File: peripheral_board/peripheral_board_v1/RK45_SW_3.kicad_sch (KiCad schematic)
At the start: 10 parts

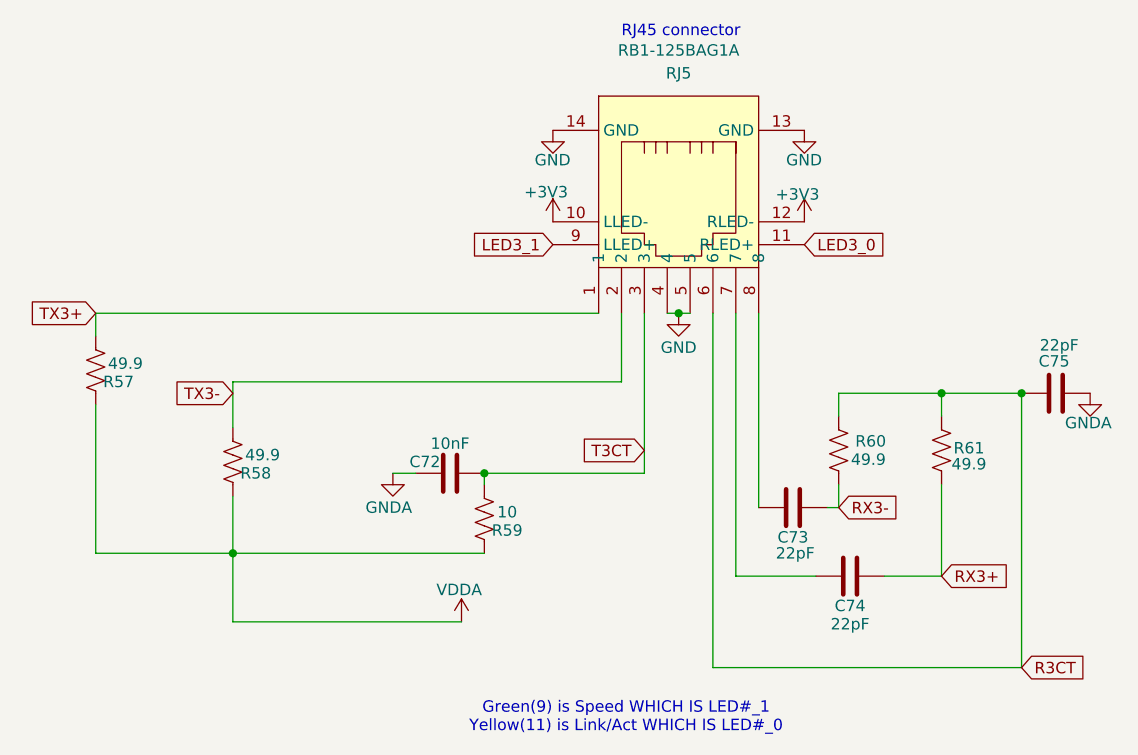
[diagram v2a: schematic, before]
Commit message: Schematic design ready for review
Made the last changes for the Wiznet by adding in Dip switches and made sure that the interrupt and reset signals are attached to the raspberry pi.

Finished the Etherent switch by wiring the RJ45 port 1 with 2 configurations, leaning more towards not using the Wiznet port but might do it any ways for cost. Added test points to port 5 but might change it to be RMII configuration because the 4 port strap in mode sets it to that config. Put solder jumpers in for the LED strap in mode. On the schematic I put in a note about how to configure to the proper mode we want but after a review will change to be a hardwire set. Made the reset switch match that of the EVAL board but further reading found I do not need the diode. Created the VDDIO and VDDAT which are just 2 different versions of 3.3V. Layout would be next but need to learn more about trace integrity and impedance control.
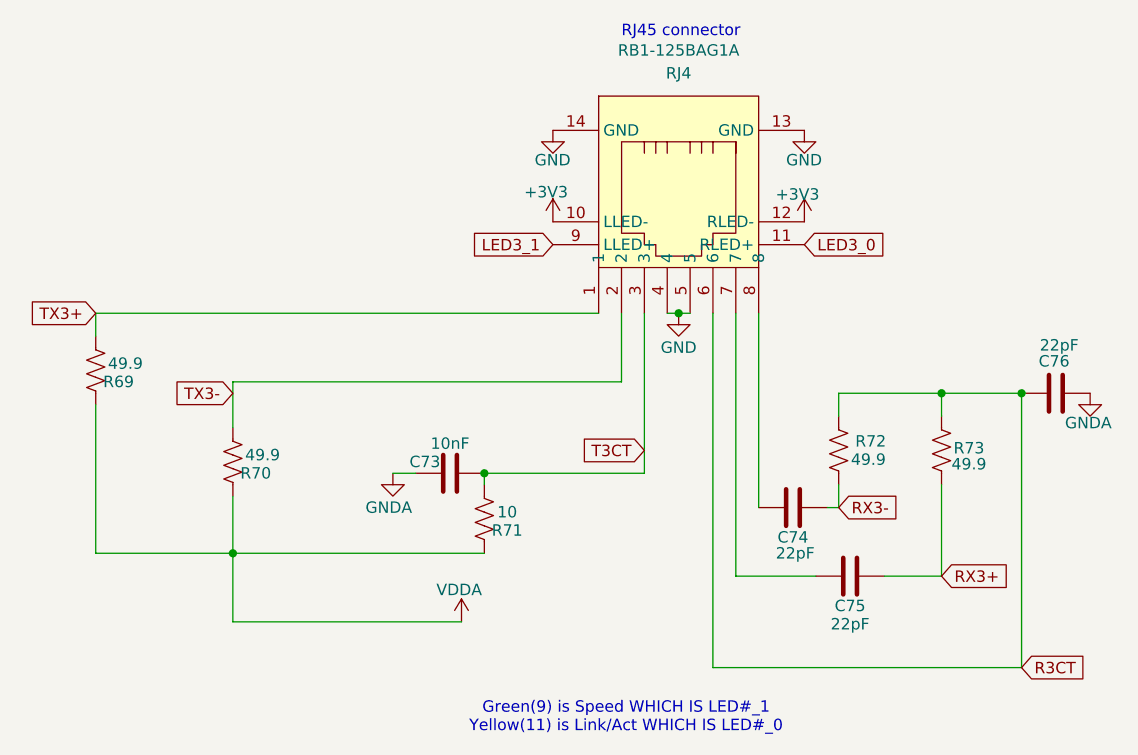
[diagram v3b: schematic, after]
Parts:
- renumbered C72 to C73, C73 to C74, C74 to C75, C75 to C76, R57 to R69, R58 to R70, R59 to R71, R60 to R72, R61 to R73, RJ5 to RJ4
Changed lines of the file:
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@@
 		(on_board yes)
 		(dnp no)
-		(property "Reference" "#PWR0139"
+		(property "Reference" "#PWR0162"
 			(at 236.22 123.19 0)
 			(effects
@@
 			(project "peripheral_board"
 				(path "/14f8712f-1710-40cb-b01e-cc9b3c4405bd/bdffb641-9271-40a7-b849-e20d9ae38619/bd5ccff9-e43e-4cae-813e-2c44e5ae50a7"
-					(reference "#PWR0139")
+					(reference "#PWR0162")
 					(unit 1)
 				)
@@
 		(on_board yes)
 		(dnp no)
-		(property "Reference" "R60"
+		(property "Reference" "R72"
 			(at 257.556 131.064 0)
 			(effects
@@
 			(project "peripheral_board"
 				(path "/14f8712f-1710-40cb-b01e-cc9b3c4405bd/bdffb641-9271-40a7-b849-e20d9ae38619/bd5ccff9-e43e-4cae-813e-2c44e5ae50a7"
-					(reference "R60")
+					(reference "R72")
 					(unit 1)
 				)
@@
 		(on_board yes)
 		(dnp no)
-		(property "Reference" "R57"
+		(property "Reference" "R69"
 			(at 173.99 124.46 0)
 			(effects
@@
 			(project "peripheral_board"
 				(path "/14f8712f-1710-40cb-b01e-cc9b3c4405bd/bdffb641-9271-40a7-b849-e20d9ae38619/bd5ccff9-e43e-4cae-813e-2c44e5ae50a7"
-					(reference "R57")
+					(reference "R69")
 					(unit 1)
 				)
@@
 		(dnp no)
 		(fields_autoplaced yes)
-		(property "Reference" "RJ5"
+		(property "Reference" "RJ4"
 			(at 236.22 90.17 0)
 			(effects
@@
 			(project "peripheral_board"
 				(path "/14f8712f-1710-40cb-b01e-cc9b3c4405bd/bdffb641-9271-40a7-b849-e20d9ae38619/bd5ccff9-e43e-4cae-813e-2c44e5ae50a7"
-					(reference "RJ5")
+					(reference "RJ4")
 					(unit 1)
 				)
@@
 		(on_board yes)
 		(dnp no)
-		(property "Reference" "C74"
+		(property "Reference" "C75"
 			(at 255.27 149.352 90)
 			(effects
@@
 			(project "peripheral_board"
 				(path "/14f8712f-1710-40cb-b01e-cc9b3c4405bd/bdffb641-9271-40a7-b849-e20d9ae38619/bd5ccff9-e43e-4cae-813e-2c44e5ae50a7"
-					(reference "C74")
+					(reference "C75")
 					(unit 1)
 				)
@@
 		(on_board yes)
 		(dnp no)
-		(property "Reference" "C75"
+		(property "Reference" "C76"
 			(at 279.654 122.174 90)
 			(effects
@@
 			(project "peripheral_board"
 				(path "/14f8712f-1710-40cb-b01e-cc9b3c4405bd/bdffb641-9271-40a7-b849-e20d9ae38619/bd5ccff9-e43e-4cae-813e-2c44e5ae50a7"
-					(reference "C75")
+					(reference "C76")
 					(unit 1)
 				)
@@
 		(on_board yes)
 		(dnp no)
-		(property "Reference" "R58"
+		(property "Reference" "R70"
 			(at 189.23 134.62 0)
 			(effects
@@
 			(project "peripheral_board"
 				(path "/14f8712f-1710-40cb-b01e-cc9b3c4405bd/bdffb641-9271-40a7-b849-e20d9ae38619/bd5ccff9-e43e-4cae-813e-2c44e5ae50a7"
-					(reference "R58")
+					(reference "R70")
 					(unit 1)
 				)
@@
 		(on_board yes)
 		(dnp no)
-		(property "Reference" "#PWR0137"
+		(property "Reference" "#PWR0160"
 			(at 222.25 102.87 0)
 			(effects
@@
 			(project "peripheral_board"
 				(path "/14f8712f-1710-40cb-b01e-cc9b3c4405bd/bdffb641-9271-40a7-b849-e20d9ae38619/bd5ccff9-e43e-4cae-813e-2c44e5ae50a7"
-					(reference "#PWR0137")
+					(reference "#PWR0160")
 					(unit 1)
 				)
@@
 		(on_board yes)
 		(dnp no)
-		(property "Reference" "R59"
+		(property "Reference" "R71"
 			(at 217.17 140.97 0)
 			(effects
@@
 			(project "peripheral_board"
 				(path "/14f8712f-1710-40cb-b01e-cc9b3c4405bd/bdffb641-9271-40a7-b849-e20d9ae38619/bd5ccff9-e43e-4cae-813e-2c44e5ae50a7"
-					(reference "R59")
+					(reference "R71")
 					(unit 1)
 				)
@@
 		(on_board yes)
 		(dnp no)
-		(property "Reference" "#PWR0141"
+		(property "Reference" "#PWR0164"
 			(at 250.19 110.49 0)
 			(effects
@@
 			(project "peripheral_board"
 				(path "/14f8712f-1710-40cb-b01e-cc9b3c4405bd/bdffb641-9271-40a7-b849-e20d9ae38619/bd5ccff9-e43e-4cae-813e-2c44e5ae50a7"
-					(reference "#PWR0141")
+					(reference "#PWR0164")
 					(unit 1)
 				)
@@
 		(on_board yes)
 		(dnp no)
-		(property "Reference" "#PWR0136"
+		(property "Reference" "#PWR0159"
 			(at 212.09 154.94 0)
 			(effects
@@
 			(project "peripheral_board"
 				(path "/14f8712f-1710-40cb-b01e-cc9b3c4405bd/bdffb641-9271-40a7-b849-e20d9ae38619/bd5ccff9-e43e-4cae-813e-2c44e5ae50a7"
-					(reference "#PWR0136")
+					(reference "#PWR0159")
 					(unit 1)
 				)
@@
 		(on_board yes)
 		(dnp no)
-		(property "Reference" "#PWR0138"
+		(property "Reference" "#PWR0161"
 			(at 222.25 110.49 0)
 			(effects
@@
 			(project "peripheral_board"
 				(path "/14f8712f-1710-40cb-b01e-cc9b3c4405bd/bdffb641-9271-40a7-b849-e20d9ae38619/bd5ccff9-e43e-4cae-813e-2c44e5ae50a7"
-					(reference "#PWR0138")
+					(reference "#PWR0161")
 					(unit 1)
 				)
@@
 		(on_board yes)
 		(dnp no)
-		(property "Reference" "C73"
+		(property "Reference" "C74"
 			(at 248.92 141.732 90)
 			(effects
@@
 			(project "peripheral_board"
 				(path "/14f8712f-1710-40cb-b01e-cc9b3c4405bd/bdffb641-9271-40a7-b849-e20d9ae38619/bd5ccff9-e43e-4cae-813e-2c44e5ae50a7"
-					(reference "C73")
+					(reference "C74")
 					(unit 1)
 				)
@@
 		(on_board yes)
 		(dnp no)
-		(property "Reference" "R61"
+		(property "Reference" "R73"
 			(at 268.478 131.826 0)
 			(effects
@@
 			(project "peripheral_board"
 				(path "/14f8712f-1710-40cb-b01e-cc9b3c4405bd/bdffb641-9271-40a7-b849-e20d9ae38619/bd5ccff9-e43e-4cae-813e-2c44e5ae50a7"
-					(reference "R61")
+					(reference "R73")
 					(unit 1)
 				)
@@
 		(on_board yes)
 		(dnp no)
-		(property "Reference" "#PWR0142"
+		(property "Reference" "#PWR0165"
 			(at 281.94 132.08 0)
 			(effects
@@
 			(project "peripheral_board"
 				(path "/14f8712f-1710-40cb-b01e-cc9b3c4405bd/bdffb641-9271-40a7-b849-e20d9ae38619/bd5ccff9-e43e-4cae-813e-2c44e5ae50a7"
-					(reference "#PWR0142")
+					(reference "#PWR0165")
 					(unit 1)
 				)
@@
 		(on_board yes)
 		(dnp no)
-		(property "Reference" "C72"
+		(property "Reference" "C73"
 			(at 208.026 133.35 90)
 			(effects
@@
 			(project "peripheral_board"
 				(path "/14f8712f-1710-40cb-b01e-cc9b3c4405bd/bdffb641-9271-40a7-b849-e20d9ae38619/bd5ccff9-e43e-4cae-813e-2c44e5ae50a7"
-					(reference "C72")
+					(reference "C73")
 					(unit 1)
 				)
@@
 		(on_board yes)
 		(dnp no)
-		(property "Reference" "#PWR0135"
+		(property "Reference" "#PWR0158"
 			(at 204.47 140.97 0)
 			(effects
@@
 			(project "peripheral_board"
 				(path "/14f8712f-1710-40cb-b01e-cc9b3c4405bd/bdffb641-9271-40a7-b849-e20d9ae38619/bd5ccff9-e43e-4cae-813e-2c44e5ae50a7"
-					(reference "#PWR0135")
+					(reference "#PWR0158")
 					(unit 1)
 				)
@@
 		(on_board yes)
 		(dnp no)
-		(property "Reference" "#PWR0140"
+		(property "Reference" "#PWR0163"
 			(at 250.19 102.87 0)
 			(effects
@@
 			(project "peripheral_board"
 				(path "/14f8712f-1710-40cb-b01e-cc9b3c4405bd/bdffb641-9271-40a7-b849-e20d9ae38619/bd5ccff9-e43e-4cae-813e-2c44e5ae50a7"
-					(reference "#PWR0140")
-					(unit 1)
-				)
+					(reference "#PWR0163")
+					(unit 1)
+				)

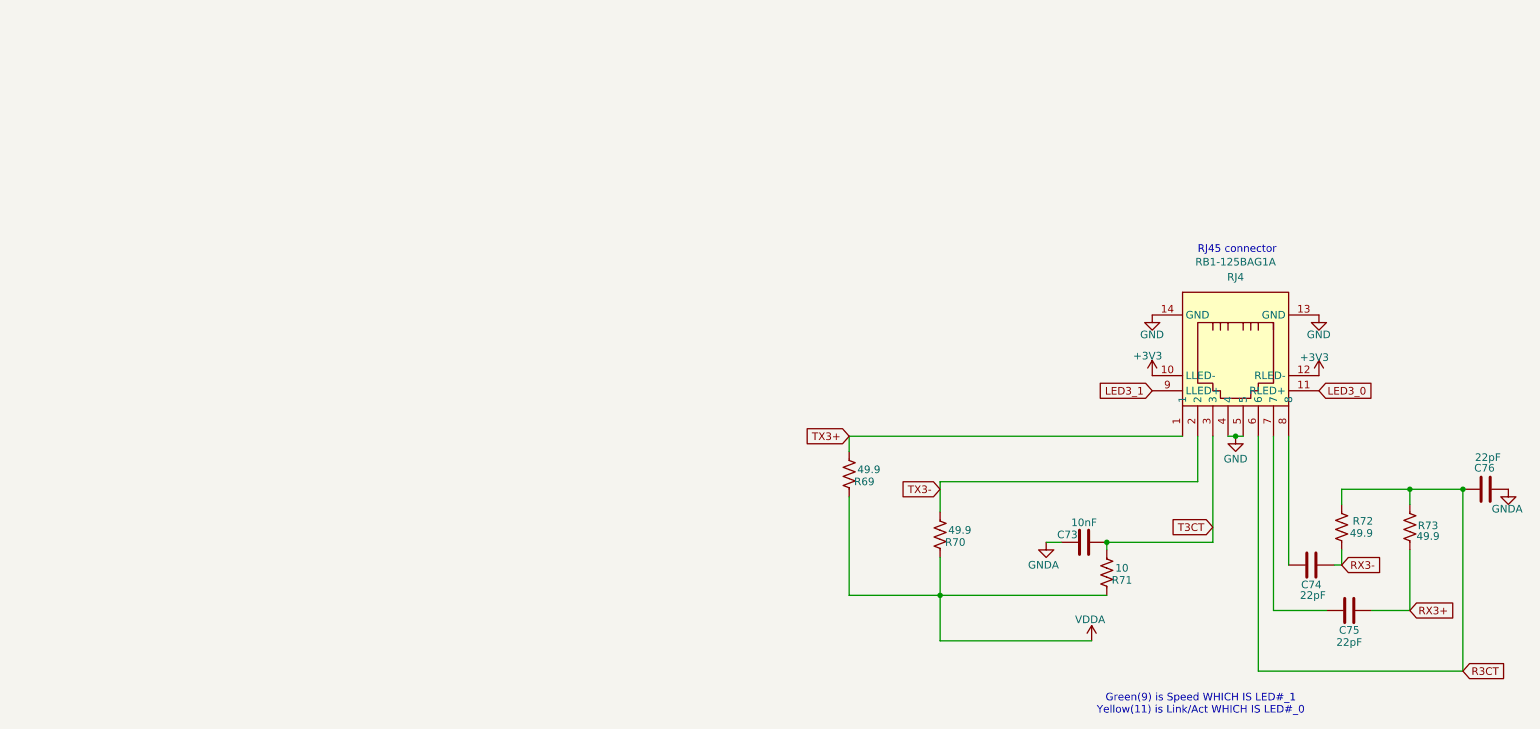
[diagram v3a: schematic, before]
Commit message: Started the PCB layout
Finished the schematic. Now working on the PCB. Might looking in to moving to a 6 layer board.
Need to do a bit of redesign because changing some of the parts had different footprints.

Started on the Wiznet and the its RJ45 port it has. Want to make the port close to the chip as a possible. Currently working on the 4 layer stack up but if I switch to a 6 layer it might help with impedance and change the overall signal layering.
Almost done with the Wiznet just need to do the clock and the TX/RX pairs.
Once that is done I will work on the Ethernet switch then lastly the breakout pins for the RP.

I should have selected either a 6 layer or 4 layer board, leaning more towards 6 layer because I can keep my signals separated by the 3 and 3 sections.
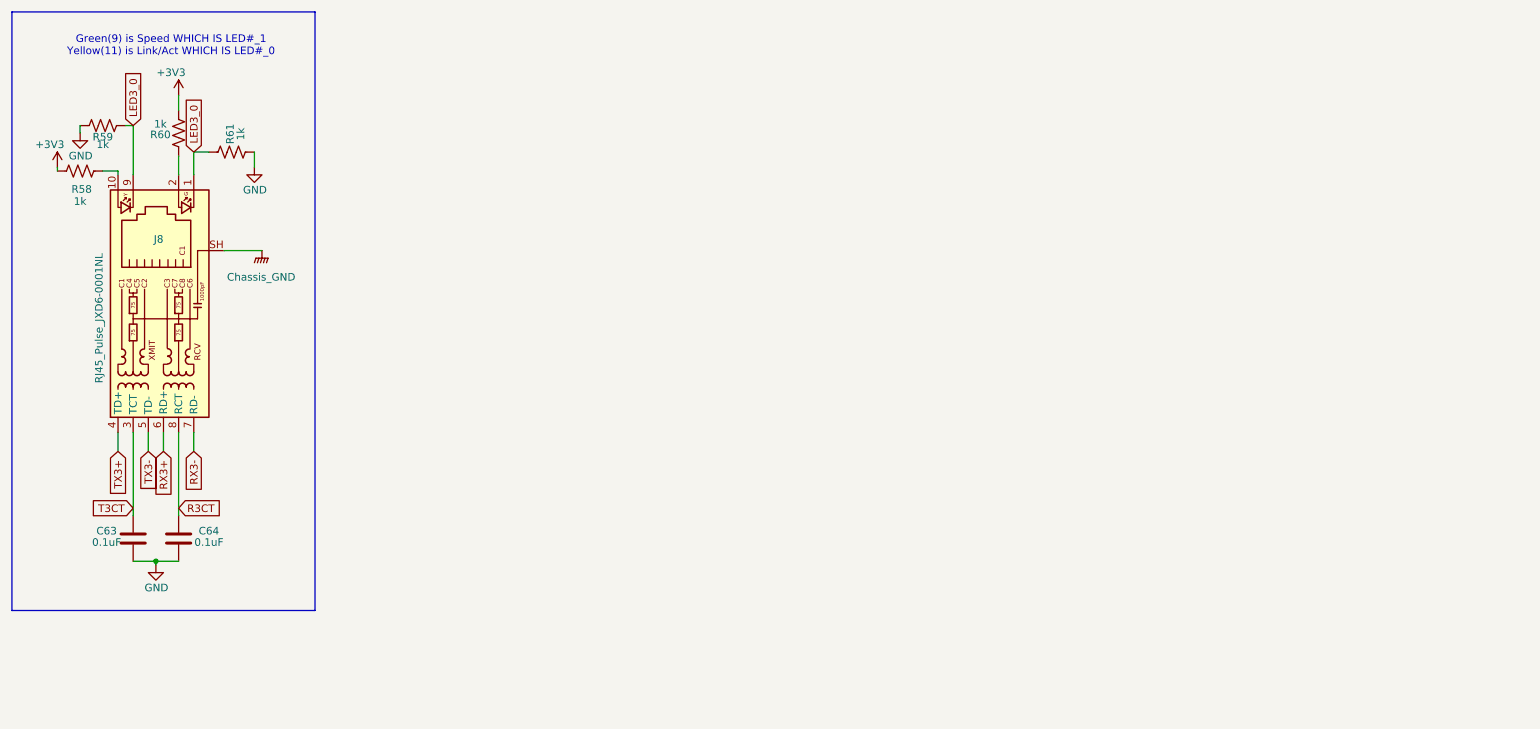
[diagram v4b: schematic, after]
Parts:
- removed C73: 10nF, Capacitor_SMD:C_0402_1005Metric, symbol Device:C
- removed C74, C75, C76: 22pF, Capacitor_SMD:C_0402_1005Metric, symbol Device:C
- removed R69, R70, R72, R73: 49.9, Resistor_SMD:R_0603_1608Metric, symbol Device:R_US
- removed R71: 10, Resistor_SMD:R_0603_1608Metric, symbol Device:R_US
- removed RJ4: RB1-125BAG1A, easyeda2kicad:RJ45-TH_RB1-125BAG1A, symbol easyeda2kicad:RB1-125BAG1A
- added C63, C64: 0.1uF, Capacitor_SMD:C_0402_1005Metric, symbol Device:C
- added J8: RJ45_Pulse_JXD6-0001NL, Connector_RJ:RJ45_Pulse_JXD6-0001NL_Horizontal, symbol Connector:RJ45_Pulse_JXD6-0001NL
- added R58, R59, R60, R61: 1k, Resistor_SMD:R_0603_1608Metric, symbol Device:R_US
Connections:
- net +3V3: now also R58.2, R60.2
- net GND: now also C63.2, C64.2, R59.2, R61.2
- net LED3_0: now also J8.1, J8.9, R59.1, R61.1
- net R3CT: now also C64.1, J8.8 (RCT)
- net RX3+: now also J8.6 (RD+)
- net RX3-: now also J8.7 (RD-)
- net T3CT: now also C63.1, J8.3 (TCT)
- net TX3+: now also J8.4 (TD+)
- net TX3-: now also J8.5 (TD-)
- new net: J8.10, R58.1
- new net: J8.2, R60.1
- new net Chassis_GND: J8.SH
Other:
- note removed: "RJ45 connector"
